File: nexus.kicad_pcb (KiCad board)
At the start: 2 copper layers, 131.5 x 147.5 mm, 111 parts, among them J1 Screw_Terminal_01x04, J10 Valve_5_PWR, J11 Valve_6_PWR, J12 24V_Lockout_Key_Switch, J13 Ignitor Screw Terminal, J14 PT_1, J15 PT_2, J16 PT_3, J17 PT_4, J18 PT_5, J19 PT_6, J2 Screw_Terminal_01x02, J20 PIN6-9_Breakout, J21 PIN10-13_Breakout, J3 4-Pin Load Cell, J4 5-Pin Load Cell, J5 XT60-M, J6 Valve_1_PWR, J7 Valve_2_PWR, J8 Valve_3_PWR, J9 Valve_4_PWR, K3 G5LE-1, K4 G5LE-1, Q1 BSS138, Q2 BSS138, Q3 BSS138, Q4 BSS138, Q5 BSS138, Q6 BSS138, Q7 BSS138, Q8 BSS138, U1 ESP32-S3, U2 ADS112C04, U3 ADS112C04, U4 ADS112C04, U5 ADS112C04, U6 TPS5430DDA, U7 TPS5430DDA, U8 XC6206P332MR

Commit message: Fix J5
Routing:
- net +24V: track 390.2 -> 402.9 mm

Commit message: routing broken
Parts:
- moved C12 1.10 mm to (125.5, 62.0)
- moved C11 0.50 mm to (93.0, 55.0)
- moved C5 0.50 mm to (160.5, 131.5)
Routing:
- net LC_FILL_-: track 0.00 -> 32.6 mm
- net LC_FILL_+: track 10.1 -> 24.8 mm
- net +24V_SAFE: track 164.1 -> 152.2 mm
- net +5V: track 290.5 -> 289.1 mm
- net GND: track 184.4 -> 185.4 mm
- net +3.3V: track 84.6 -> 83.8 mm
- net +10V: track 145.7 -> 145.0 mm

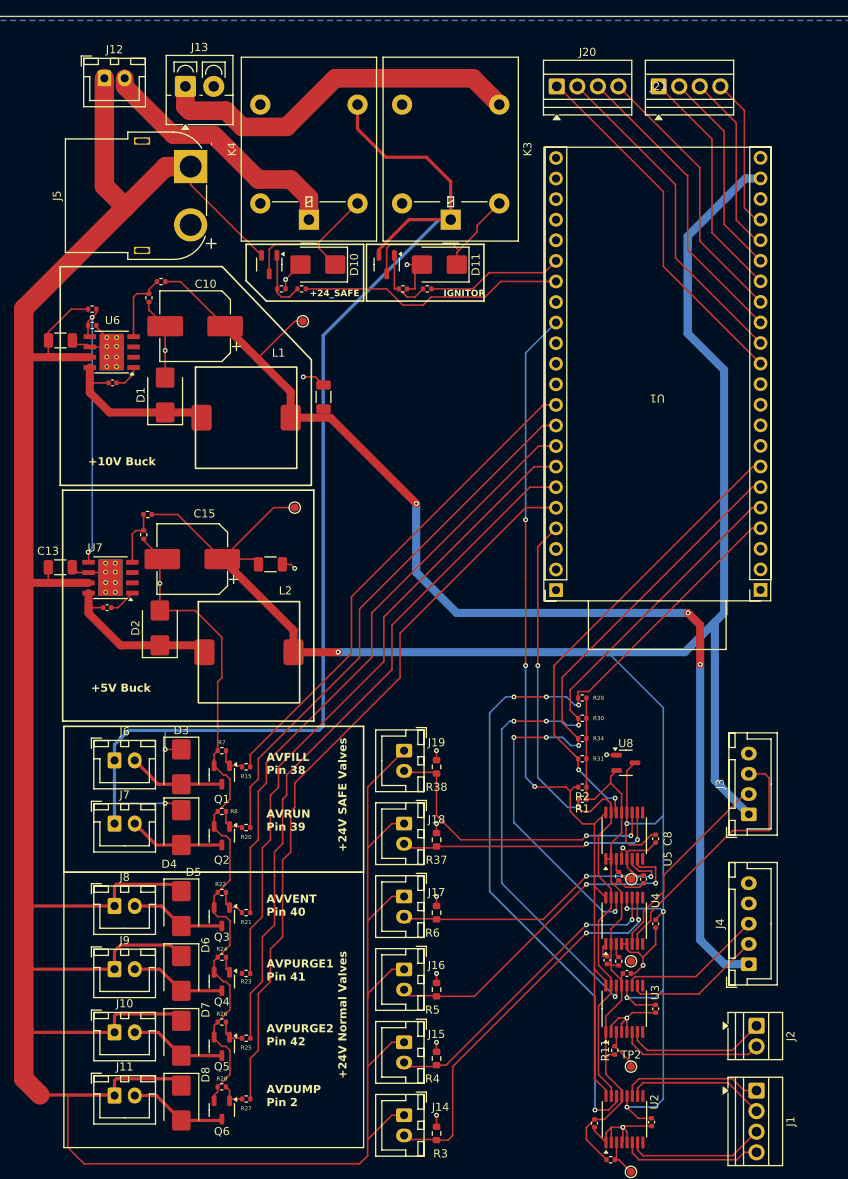
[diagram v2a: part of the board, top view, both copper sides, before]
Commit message: Fix connector references
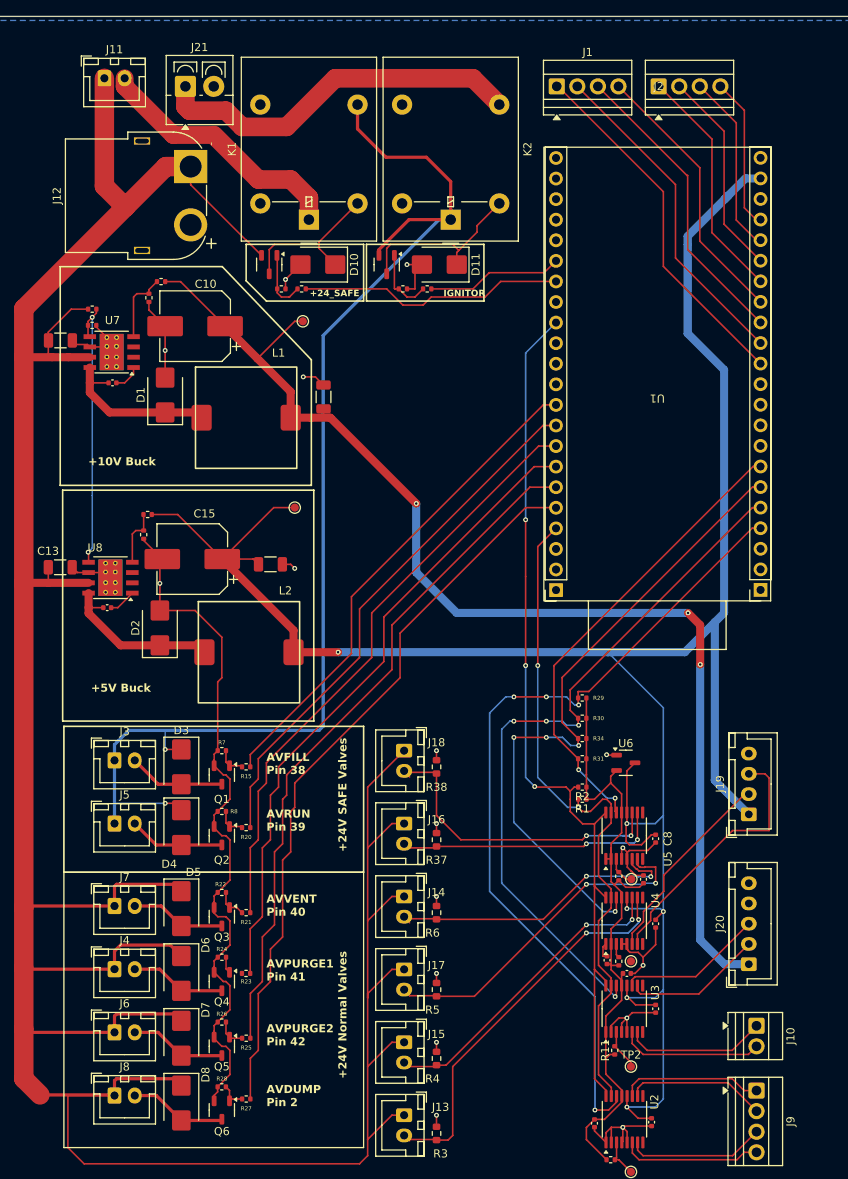
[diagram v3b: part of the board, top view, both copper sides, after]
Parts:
- renumbered J20 to J1, J2 to J10, J12 to J11, J5 to J12, J14 to J13, J17 to J14, J18 to J16, J16 to J17, J19 to J18, J3 to J19, J21 to J2, J4 to J20, J13 to J21, J6 to J3, J9 to J4, J7 to J5, J10 to J6, J8 to J7, J11 to J8, J1 to J9, K4 to K1, K3 to K2, U8 to U6, U6 to U7, U7 to U8

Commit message: Route buck converters
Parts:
- removed D11: SK44BL, Diode_SMD:D_SMB
- removed R39: 10k, Resistor_SMD:R_0402_1005Metric
- removed TP1: ADC1_RST, TestPoint:TestPoint_Pad_D1.0mm
- removed TP2: ADC2_RST, TestPoint:TestPoint_Pad_D1.0mm
- removed TP3: ADC3_RST, TestPoint:TestPoint_Pad_D1.0mm
- removed TP4: ADC4_RST, TestPoint:TestPoint_Pad_D1.0mm
- added D9: SK44BL, Diode_SMD:D_SMB, F.Cu at (259.8, 73.5)
- added R14: 100k, Resistor_SMD:R_0402_1005Metric, F.Cu at (240.9, 153.4)
- C10, C15: value 220uF -> 10uF; footprint Capacitor_SMD:CP_Elec_8x10.5 -> Capacitor_SMD:C_1206_3216Metric
- C11, C12: value 10uF -> 10nF; footprint Capacitor_SMD:C_1206_3216Metric -> Capacitor_SMD:C_0402_1005Metric
- C13: value 10uF -> 220uF; footprint Capacitor_SMD:C_1206_3216Metric -> Capacitor_SMD:CP_Elec_8x10.5
- C14: value 10nF -> 220uF; footprint Capacitor_SMD:C_0402_1005Metric -> Capacitor_SMD:CP_Elec_8x10.5
- C9: value 10nF -> 10uF; footprint Capacitor_SMD:C_0402_1005Metric -> Capacitor_SMD:C_1206_3216Metric
- R10, R9: value 10k -> 100k
- R11: value 10k -> 100
- R12: value 1.4K -> 100
- R15, R20, R25, R27: value 100 -> 10k
- R17: value 10k -> 3.3k
- R21: value 100 -> 3.3k
- R22: value 100k -> 3.3k
- R23: value 100 -> 100k
- R24: value 100k -> 10k
- R26, R7, R8: value 100k -> 100
- R28: value 100k -> 1.4K
- R29: value 3.3k -> 10k
- R3, R38, R4: value 250 -> 100; footprint Resistor_SMD:R_0603_1608Metric -> Resistor_SMD:R_0402_1005Metric
- R31, R34: value 3.3k -> 250; footprint Resistor_SMD:R_0402_1005Metric -> Resistor_SMD:R_0603_1608Metric
- R32, R35: value 10k -> 250; footprint Resistor_SMD:R_0402_1005Metric -> Resistor_SMD:R_0603_1608Metric
- R33, R36: value 100 -> 250; footprint Resistor_SMD:R_0402_1005Metric -> Resistor_SMD:R_0603_1608Metric
- R37: value 250 -> 10k; footprint Resistor_SMD:R_0603_1608Metric -> Resistor_SMD:R_0402_1005Metric
- R5, R6: value 250 -> 100k; footprint Resistor_SMD:R_0603_1608Metric -> Resistor_SMD:R_0402_1005Metric
- moved R13 175.5 mm to (240.9, 151.4)
- moved D7 171.1 mm to (259.8, 62.4), turned to 0 degrees
- moved R10 169.6 mm to (238.0, 153.4), turned to 0 degrees
- moved R12 169.4 mm to (240.9, 149.5), turned to 0 degrees
- moved R26 168.9 mm to (265.5, 66.5), turned to 0 degrees
- moved R25 168.0 mm to (265.5, 64.6), turned to 0 degrees
- moved D10 167.5 mm to (271.5, 126.6), turned to 0 degrees
- moved R24 167.2 mm to (265.5, 62.6), turned to 0 degrees
- moved R23 166.2 mm to (265.5, 60.6), turned to 0 degrees
- moved J13 162.7 mm to (272.5, 63.0), turned to 0 degrees
- moved U8 161.6 mm to (260.5, 93.8), turned to 0 degrees
- moved Q8 161.4 mm to (269.8, 131.7), turned to 0 degrees
- moved R32 160.9 mm to (280.5, 63.4)
- moved R33 158.7 mm to (280.5, 65.9)
- moved C10 157.2 mm to (259.1, 102.1), turned to 0 degrees
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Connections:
- C10 pad 1: +10V -> +24V
- C11 pad 1: +24V -> /Power Regulation/+10V_REG_BOOT
- C11 pad 2: GND -> /Power Regulation/+10V_REG_PH
- C12 pad 1: +10V -> Net-(U8-BOOT)
- C12 pad 2: GND -> Net-(D9-K)
- C13 pad 1: +24V -> +10V
- C14 pad 1: Net-(U7-BOOT) -> +5V
- C14 pad 2: Net-(D2-K) -> GND
- C15 pad 1: +5V -> +10V
- C2 pad 1: +5V -> +3.3V
- C3 pad 1: +3.3V -> +5V
- C6 pad 1: +5V -> +3.3V
- C7 pad 1: +3.3V -> +5V
- C9 pad 1: /Power Regulation/+10V_REG_BOOT -> +24V
- C9 pad 2: /Power Regulation/+10V_REG_PH -> GND
- D1 pad 1: /Power Regulation/+10V_REG_PH -> +24V_SAFE
- D1 pad 2: GND -> VALVE_1_RET
- D10 pad 1: /Power Regulation/LOCKOUT_RLY_+VE -> /Ignitor Control/IGNITOR_RLY_+VE
- D2 pad 1: Net-(D2-K) -> +24V
- D2 pad 2: GND -> VALVE_4_RET
- D3 pad 2: VALVE_1_RET -> VALVE_2_RET
- D4 pad 1: +24V_SAFE -> +24V
- D4 pad 2: VALVE_2_RET -> VALVE_5_RET
- D6 pad 2: VALVE_4_RET -> VALVE_6_RET
- D7 pad 1: +24V -> /Power Regulation/LOCKOUT_RLY_+VE
- D7 pad 2: VALVE_5_RET -> GND
- D8 pad 1: +24V -> /Power Regulation/+10V_REG_PH
- D8 pad 2: VALVE_6_RET -> GND
- L2 pad 1: Net-(D2-K) -> Net-(D9-K)
- Q2 pad 3: VALVE_2_RET -> VALVE_4_RET
- Q3 pad 3: VALVE_3_RET -> VALVE_2_RET
- Q4 pad 3: VALVE_4_RET -> VALVE_5_RET
- Q5 pad 3: VALVE_5_RET -> VALVE_3_RET
- R10 pad 1: +10V -> Net-(Q4-G)
- R10 pad 2: /Power Regulation/+10V_SENSE -> GND
- R11 pad 1: +3.3V -> VALVE_3_CTL
- R11 pad 2: Net-(U3-RESET) -> Net-(Q5-G)
- R12 pad 1: /Power Regulation/+10V_SENSE -> VALVE_6_CTL
- R12 pad 2: GND -> Net-(Q6-G)
- R13 pad 1: +24V -> Net-(Q5-G)
- R13 pad 2: /Power Regulation/VREG_EN -> GND
- R15 pad 1: VALVE_1_CTL -> +3.3V
- R15 pad 2: Net-(Q1-G) -> Net-(U2-RESET)
- R16 pad 2: Net-(U2-RESET) -> Net-(U3-RESET)
- R17 pad 2: Net-(U4-RESET) -> I2C_DRDY_ADC1
- R18 pad 1: Net-(U7-VSENSE) -> +3.3V
- R18 pad 2: GND -> I2C_DRDY_ADC2
- R19 pad 2: Net-(U5-RESET) -> Net-(U4-RESET)
- R20 pad 1: VALVE_2_CTL -> +3.3V
- R20 pad 2: Net-(Q2-G) -> Net-(U5-RESET)
- R21 pad 1: VALVE_3_CTL -> +3.3V
- R21 pad 2: Net-(Q3-G) -> I2C_DRDY_ADC4
- R22 pad 1: Net-(Q3-G) -> +3.3V
- R22 pad 2: GND -> I2C_DRDY_ADC3
- R23 pad 1: VALVE_4_CTL -> +24V
- R23 pad 2: Net-(Q4-G) -> /Power Regulation/VREG_EN
- R24 pad 1: Net-(Q4-G) -> /Power Regulation/VREG_EN
- R25 pad 1: VALVE_5_CTL -> /Power Regulation/LOCKOUT_RLY_CTRL_FET
- R25 pad 2: Net-(Q5-G) -> GND
- R26 pad 1: Net-(Q5-G) -> /Power Regulation/LOCKOUT_RLY_CTRL_FET
- R26 pad 2: GND -> SAFE_24V_CTL
- R27 pad 1: VALVE_6_CTL -> +10V
- R27 pad 2: Net-(Q6-G) -> /Power Regulation/+10V_SENSE
- R28 pad 1: Net-(Q6-G) -> /Power Regulation/+10V_SENSE
- R29 pad 1: +3.3V -> +5V
- R29 pad 2: I2C_DRDY_ADC1 -> Net-(U8-VSENSE)
- R3 pad 1: PT_READING_1 -> VALVE_1_CTL
- R3 pad 2: GND -> Net-(Q1-G)
- R30 pad 1: +3.3V -> Net-(U8-VSENSE)
- R30 pad 2: I2C_DRDY_ADC2 -> GND
- R31 pad 1: +3.3V -> PT_READING_1
- R31 pad 2: I2C_DRDY_ADC4 -> GND
- R32 pad 1: /Power Regulation/LOCKOUT_RLY_CTRL_FET -> PT_READING_4
- R33 pad 1: /Power Regulation/LOCKOUT_RLY_CTRL_FET -> PT_READING_2
- R33 pad 2: SAFE_24V_CTL -> GND
- R34 pad 1: +3.3V -> PT_READING_5
- R34 pad 2: I2C_DRDY_ADC3 -> GND
- R35 pad 1: /Ignitor Control/IGNITOR_CTL_FET -> PT_READING_3
- R36 pad 1: /Ignitor Control/IGNITOR_CTL_FET -> PT_READING_6
- R36 pad 2: IGNITOR_CTL -> GND
- R37 pad 1: PT_READING_5 -> /Ignitor Control/IGNITOR_CTL_FET
- R38 pad 1: PT_READING_6 -> /Ignitor Control/IGNITOR_CTL_FET
- R38 pad 2: GND -> IGNITOR_CTL
- R4 pad 1: PT_READING_2 -> VALVE_4_CTL
- R4 pad 2: GND -> Net-(Q2-G)
- R5 pad 1: PT_READING_3 -> Net-(Q1-G)
- R6 pad 1: PT_READING_4 -> Net-(Q2-G)
- R7 pad 1: Net-(Q1-G) -> VALVE_2_CTL
- R7 pad 2: GND -> Net-(Q3-G)
- R8 pad 1: Net-(Q2-G) -> VALVE_5_CTL
- R8 pad 2: GND -> Net-(Q4-G)
- R9 pad 1: +5V -> Net-(Q3-G)
- R9 pad 2: Net-(U7-VSENSE) -> GND
- U1 pad 41: VALVE_4_CTL -> (no net)
- U8 pad 1: Net-(U7-BOOT) -> Net-(U8-BOOT)
- U8 pad 4: Net-(U7-VSENSE) -> Net-(U8-VSENSE)
- U8 pad 8: Net-(D2-K) -> Net-(D9-K)
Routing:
- net +24V: track 403.3 -> 0.00 mm
- net +5V: track 289.1 -> 0.00 mm, vias 6 -> 0
- net GND: track 185.4 -> 9.04 mm, vias 17 -> 0
- net +24V_SAFE: track 152.2 -> 0.00 mm, vias 2 -> 0
- net +10V: track 145.0 -> 18.8 mm, vias 3 -> 0
- net I2C_SCL: track 112.2 -> 0.00 mm, vias 3 -> 0
- net I2C_DRDY_ADC1: track 103.0 -> 0.00 mm, vias 4 -> 0
- net VALVE_6_CTL: track 90.8 -> 0.00 mm
- net I2C_DRDY_ADC2: track 88.0 -> 0.00 mm, vias 4 -> 0
- net VALVE_5_CTL: track 85.5 -> 0.00 mm
- net I2C_SDA: track 84.3 -> 0.00 mm, vias 2 -> 0
- net +3.3V: track 83.8 -> 0.00 mm
- net I2C_DRDY_ADC3: track 81.2 -> 0.00 mm, vias 4 -> 0
- net VALVE_4_CTL: track 79.8 -> 0.00 mm
- net VALVE_3_CTL: track 74.5 -> 0.00 mm
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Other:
- board outline removed
- board text removed: "+10V Buck"
- board text removed: "+24V Normal Valves"
- board text removed: "+24V SAFE Valves"
- board text removed: "+24_SAFE"
- board text removed: "+5V Buck"
- board text removed: "AVDUMP Pin 2"
- board text removed: "AVFILL Pin 38"
- board text removed: "AVPURGE1 Pin 41"
- board text removed: "AVPURGE2 Pin 42"
- board text removed: "AVRUN Pin 39"
- board text removed: "AVVENT Pin 40"
- board text removed: "IGNITOR"

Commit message: Route first solenoid
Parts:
- moved R36 235.6 mm to (58.0, 150.8), turned to -90 degrees
- moved R35 233.6 mm to (58.0, 142.0), turned to -90 degrees
- moved R34 231.6 mm to (58.0, 132.8), turned to -90 degrees
- moved R33 230.0 mm to (58.0, 123.8), turned to -90 degrees
- moved R32 228.4 mm to (58.0, 114.7), turned to -90 degrees
- moved R31 227.0 mm to (58.0, 105.7), turned to -90 degrees
- moved J18 225.3 mm to (53.0, 152.5), turned to 90 degrees
- moved J17 225.1 mm to (53.0, 143.7), turned to 90 degrees
- moved J16 224.8 mm to (53.0, 134.5), turned to 90 degrees
- moved J15 224.5 mm to (53.0, 125.5), turned to 90 degrees
- moved J14 224.2 mm to (53.0, 116.3), turned to 90 degrees
- moved J13 224.0 mm to (53.0, 107.3), turned to 90 degrees
- moved Q7 222.1 mm to (49.4, 44.5), turned to 180 degrees
- moved Q8 220.0 mm to (67.9, 44.5), turned to 180 degrees
- moved R38 219.8 mm to (71.5, 46.5)
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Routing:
- net +24V: track 0.00 -> 83.0 mm
- net /Ignitor Control/IGNITOR_SOURCE: track 0.00 -> 49.1 mm
- net +24V_SAFE: track 0.00 -> 36.7 mm
- net /Power Regulation/+24V_POST_LOCKOUT: track 0.00 -> 34.3 mm
- net +5V: track 0.00 -> 28.6 mm
- net /Power Regulation/VREG_EN: track 0.00 -> 22.4 mm, vias 0 -> 2
- net /Ignitor Control/IGNITOR_RLY_+VE: track 0.00 -> 19.8 mm
- net /Power Regulation/LOCKOUT_RLY_+VE: track 0.00 -> 19.8 mm
- net +10V: track 18.8 -> 28.4 mm
- net Net-(D9-K): track 0.00 -> 7.59 mm
- net VALVE_1_RET: track 0.00 -> 6.77 mm
- net GND: track 9.04 -> 15.0 mm
- net PT_READING_5: track 0.00 -> 5.06 mm
- net PT_READING_6: track 0.00 -> 5.02 mm
- net PT_READING_4: track 0.00 -> 5.00 mm
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- added copper zone on F.Cu, net GND

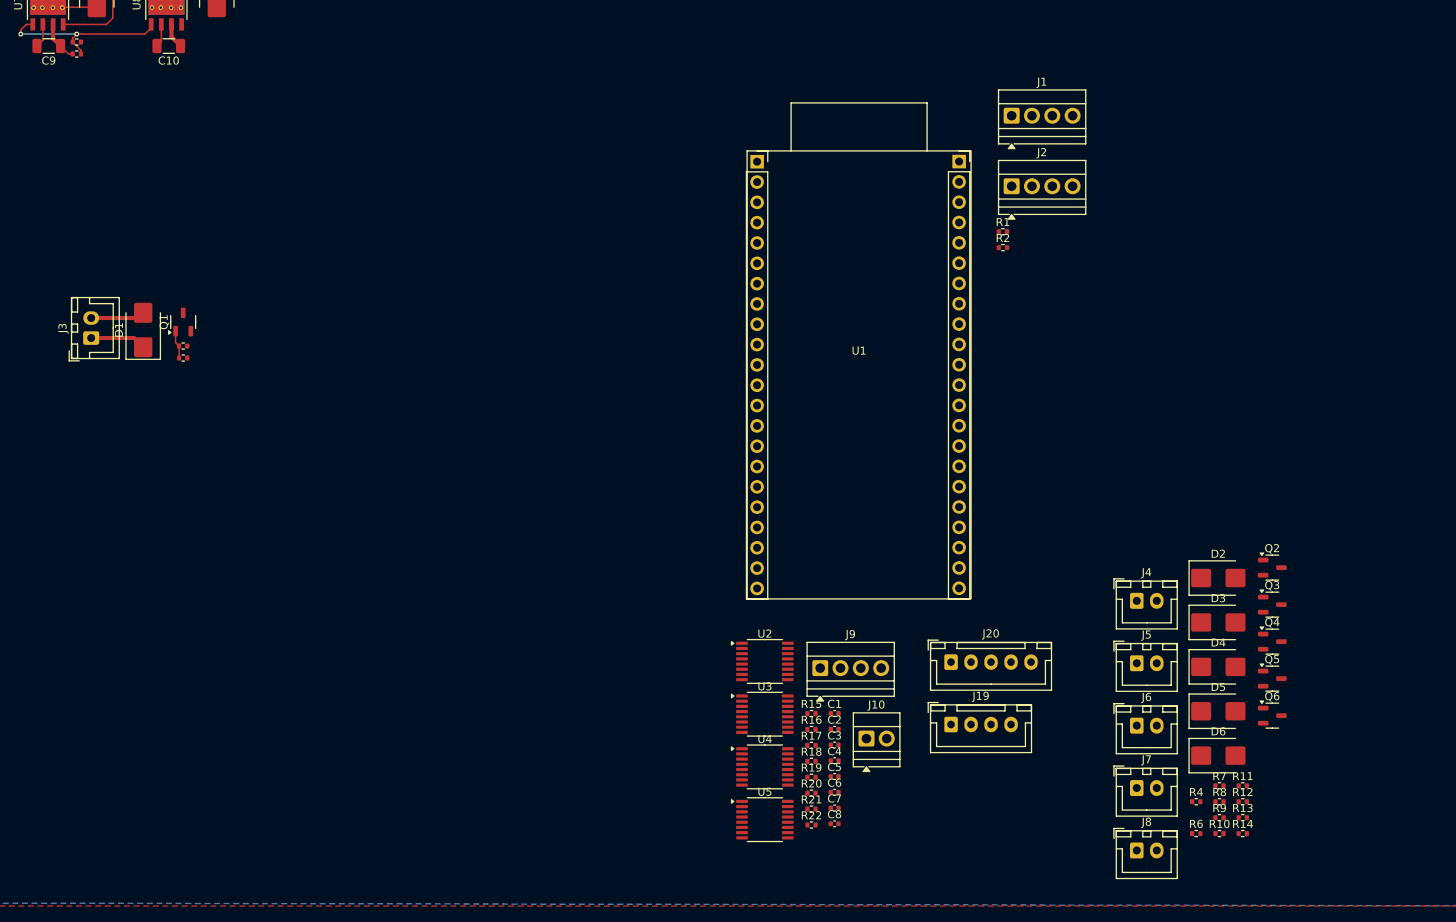
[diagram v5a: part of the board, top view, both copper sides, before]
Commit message: Route All solenoids
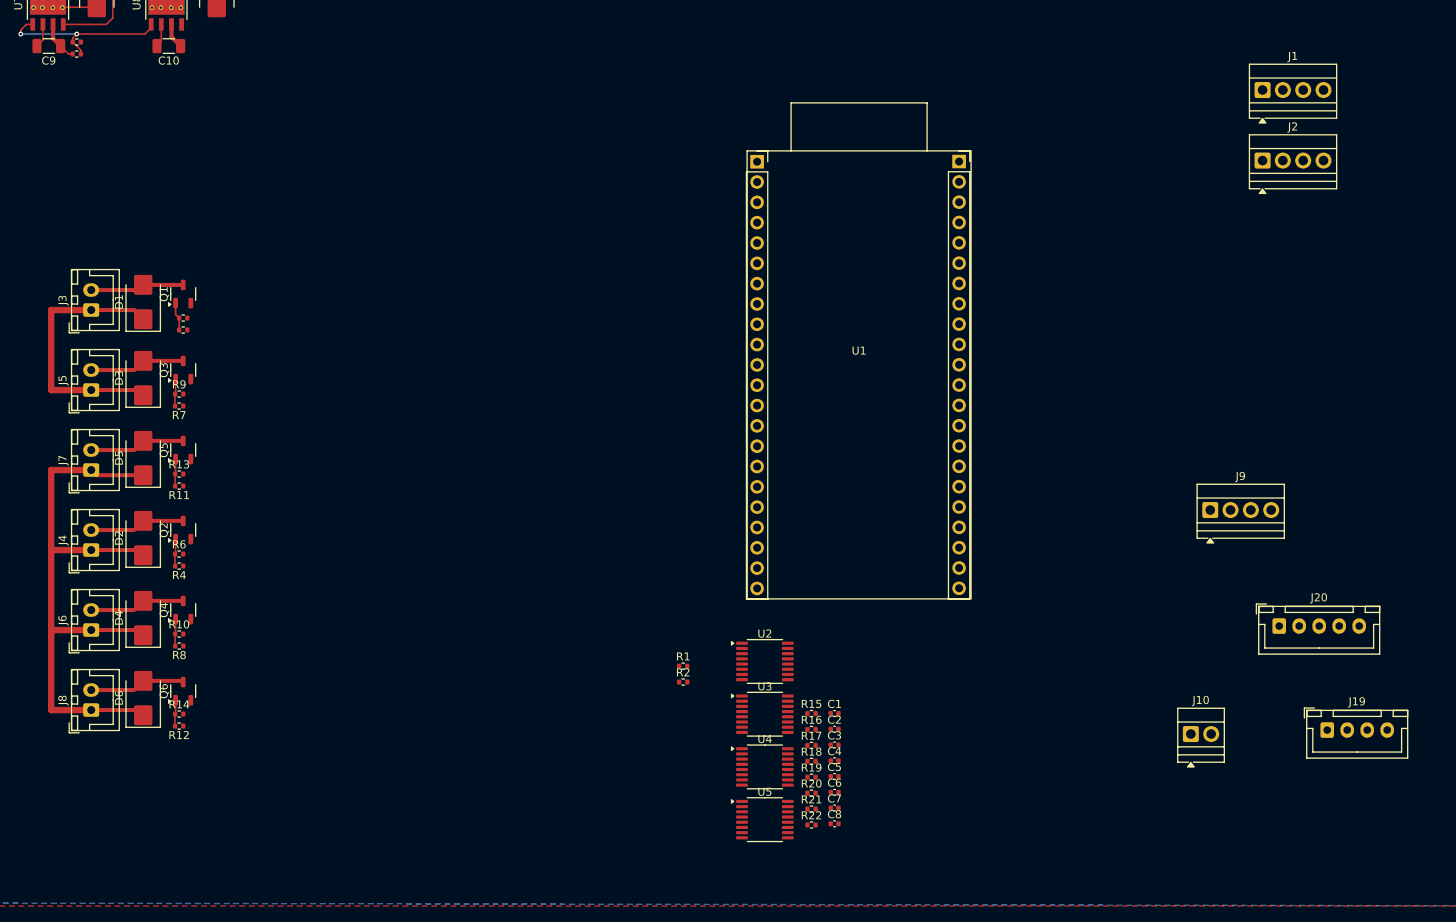
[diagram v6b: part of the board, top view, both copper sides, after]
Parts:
- moved R9 140.4 mm to (108.0, 98.5)
- moved R13 139.7 mm to (108.0, 108.5)
- moved Q3 139.3 mm to (108.5, 95.5), turned to 90 degrees
- moved Q5 139.1 mm to (108.5, 105.5), turned to 90 degrees
- moved R7 138.4 mm to (108.0, 100.0), turned to 180 degrees
- moved R11 138.1 mm to (108.0, 110.0), turned to 180 degrees
- moved D5 138.1 mm to (103.5, 106.5), turned to 90 degrees
- moved D3 137.8 mm to (103.5, 96.5), turned to 90 degrees
- moved J7 136.6 mm to (97.0, 108.0), turned to 90 degrees
- moved Q2 136.2 mm to (108.5, 115.5), turned to 90 degrees
- moved Q4 136.2 mm to (108.5, 125.5), turned to 90 degrees
- moved Q6 136.2 mm to (108.5, 135.6), turned to 90 degrees
- moved J5 135.1 mm to (97.0, 98.0), turned to 90 degrees
- moved D6 134.6 mm to (103.5, 136.5), turned to 90 degrees
- moved D4 134.5 mm to (103.5, 126.5), turned to 90 degrees
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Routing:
- net +24V: track 83.0 -> 159.6 mm
- net +24V_SAFE: track 36.7 -> 63.5 mm
- net VALVE_6_RET: track 0.00 -> 12.0 mm
- net VALVE_5_RET: track 0.00 -> 12.0 mm
- net VALVE_4_RET: track 0.00 -> 12.0 mm
- net VALVE_3_RET: track 0.00 -> 12.0 mm
- net VALVE_2_RET: track 0.00 -> 12.0 mm
- net VALVE_1_RET: track 6.77 -> 11.8 mm
- net Net-(Q2-G): track 0.00 -> 3.40 mm
- net Net-(Q4-G): track 0.00 -> 3.39 mm
- net Net-(Q3-G): track 0.00 -> 3.39 mm
- net Net-(Q5-G): track 0.00 -> 3.39 mm
- net Net-(Q6-G): track 0.00 -> 3.25 mm

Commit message: Route I2C lines and ADC communications
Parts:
- moved J19 209.8 mm to (42.0, 128.5)
- moved J9 203.5 mm to (33.5, 120.6), turned to 90 degrees
- moved J10 201.4 mm to (33.5, 128.0), turned to 90 degrees
- moved J20 189.0 mm to (56.5, 128.5)
- moved R15 132.6 mm to (58.7, 104.8), turned to 180 degrees
- moved C3 130.1 mm to (64.2, 108.8)
- moved C1 129.4 mm to (64.2, 107.8)
- moved J1 127.9 mm to (116.5, 76.4), turned to -90 degrees
- moved J2 127.0 mm to (116.5, 64.0), turned to -90 degrees
- moved R17 127.0 mm to (65.2, 106.3), turned to 90 degrees
- moved U2 124.7 mm to (58.7, 108.3)
- moved R16 120.2 mm to (72.4, 104.3), turned to 180 degrees
- moved C4 117.3 mm to (78.3, 108.3)
- moved C2 116.5 mm to (78.3, 107.3)
- moved R18 114.9 mm to (78.8, 105.8), turned to 90 degrees
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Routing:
- net +5V: track 28.6 -> 223.4 mm, vias 0 -> 6
- net +3.3V: track 0.00 -> 157.2 mm, vias 0 -> 6
- net +10V: track 28.4 -> 167.9 mm, vias 0 -> 1
- net I2C_SCL: track 0.00 -> 101.6 mm, vias 0 -> 11
- net I2C_SDA: track 0.00 -> 101.3 mm, vias 0 -> 11
- net +24V: track 159.6 -> 254.6 mm
- net I2C_DRDY_ADC4: track 0.00 -> 59.8 mm
- net I2C_DRDY_ADC3: track 0.00 -> 45.7 mm
- net +24V_SAFE: track 63.5 -> 100.3 mm
- net I2C_DRDY_ADC2: track 0.00 -> 34.4 mm
- net PT_READING_6: track 5.02 -> 32.5 mm
- net PT_READING_1: track 5.00 -> 32.1 mm
- net PT_READING_2: track 5.00 -> 28.8 mm
- net I2C_DRDY_ADC1: track 0.00 -> 23.6 mm
- net PT_READING_5: track 5.06 -> 28.5 mm
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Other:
- board text added: "AVFILL"
- board text added: "AVRUN"
